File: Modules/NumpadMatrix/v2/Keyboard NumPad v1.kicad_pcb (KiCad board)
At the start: 2 copper layers, 80.2 x 123 mm, 57 parts, among them U2 ESP32-C3_SUPERMINI_SMD

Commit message: Update of Module V2  x_x
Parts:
- added ?: , , F.Cu at (45.9, 129.1)
- added ?: , , F.Cu at (84.0, 129.0)
- added ?: , , F.Cu at (64.9, 50.9)
- D26: moved to B.Cu
- moved D22 1.54 mm to (63.7, 138.9)
- turned S21 to 180 degrees
- turned S22 to 180 degrees
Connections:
- D27 pad 1: Linha 5 -> Linha 4
- S25 pad 1: Coluna 3 -> Coluna 4
- S26 pad 1: Coluna 3 -> Coluna 4
- S27 pad 1: Coluna 0 -> Coluna 4
- U2 pad 10: unconnected-(U2-GPIO10-Pad10) -> Coluna 4
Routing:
- net Coluna 4: track 0.00 -> 180.9 mm, vias 0 -> 4
- net Linha 4: track 162.0 -> 188.2 mm, vias 1 -> 2
- net Coluna 1: track 122.9 -> 137.5 mm, vias 2 -> 4
- net Linha 5: track 267.6 -> 257.9 mm
- net Net-(D21-A): track 3.95 -> 12.4 mm
- net Net-(D22-A): track 9.75 -> 17.5 mm
- net Coluna 0: track 133.9 -> 129.2 mm, vias 1 -> 2
- net Coluna 3: track 173.0 -> 176.2 mm
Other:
- board text added: "GND"

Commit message: fuck x_x
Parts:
- moved D5 3.25 mm to (42.6, 71.4), turned to 180 degrees
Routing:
- net Linha 0: track 23.3 -> 82.8 mm
- net Linha 5: track 257.9 -> 213.5 mm
- net Coluna 0: track 129.2 -> 155.6 mm, vias 2 -> 6
- net Coluna 1: track 137.5 -> 149.8 mm, vias 4 -> 5
- net Coluna 4: track 180.9 -> 169.6 mm, vias 4 -> 6
- net Coluna 3: track 176.2 -> 183.3 mm, vias 1 -> 2
- net Net-(D16-A): track 17.3 -> 24.2 mm, vias 1 -> 2
- net Net-(D5-A): track 14.7 -> 7.79 mm
- net Net-(D11-A): track 6.40 -> 13.0 mm, vias 0 -> 1
- net Net-(D4-A): track 6.20 -> 1.42 mm
- net Coluna 2: track 148.9 -> 144.3 mm
- net Net-(D25-A): track 0.00 -> 3.38 mm
- net Net-(D12-A): track 6.20 -> 3.42 mm
- net Net-(D1-A): track 6.56 -> 3.78 mm
- net Linha 4: track 188.2 -> 185.6 mm
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- removed copper zone on B.Cu, net (none)
- removed copper zone on F.Cu, net (none)

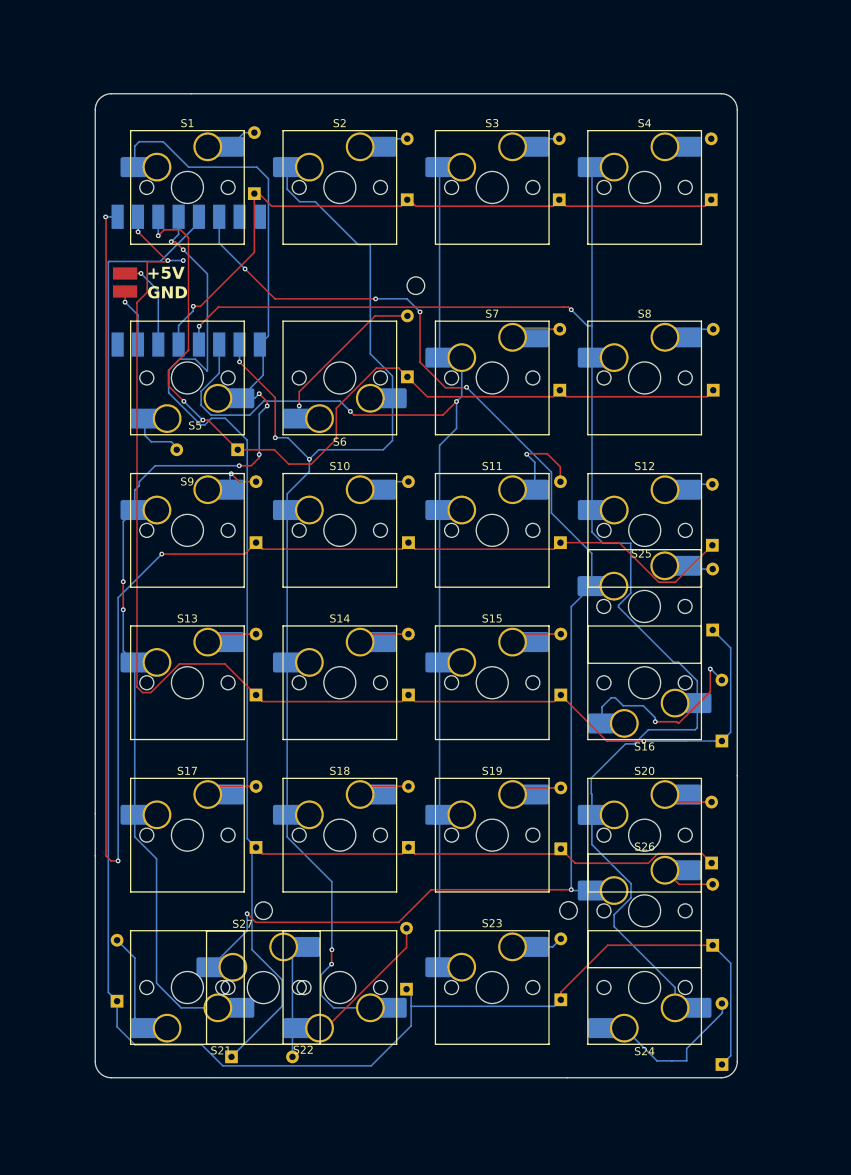
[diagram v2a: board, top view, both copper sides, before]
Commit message: Filled copper regions on the numpad module
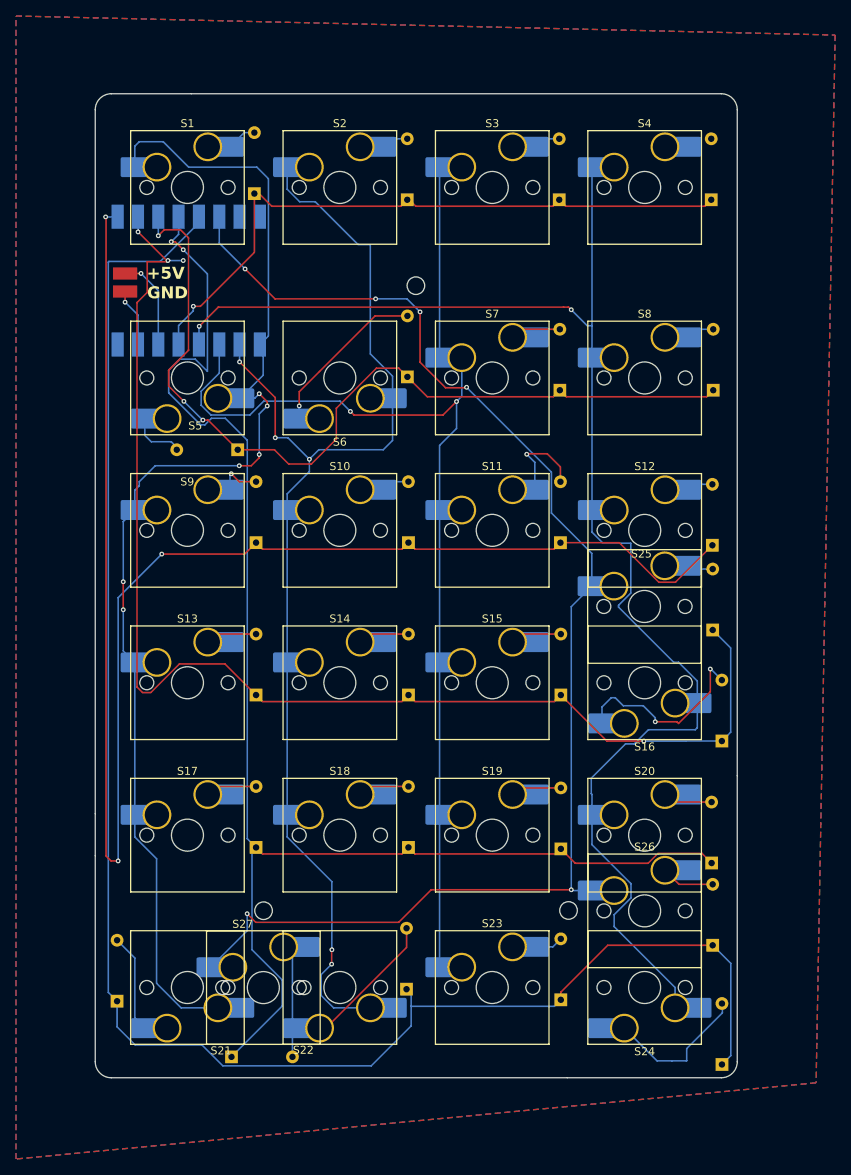
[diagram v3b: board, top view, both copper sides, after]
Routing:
- added copper zone on B.Cu, net (none)
- added copper zone on F.Cu, net (none)
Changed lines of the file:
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@@
 		(tags "Keyboard Keyswitch Switch Hotswap Socket Plated Relief Cutout Keycap 1.00u")
 		(property "Reference" "S12"
-			(at 0 -8 360)
+			(at 0 -8 0)
 			(layer "F.SilkS")
 			(effects
@@
 		)
 		(property "Value" "Keyswitch"
-			(at 0 8 360)
+			(at 0 8 0)
 			(layer "F.Fab")
 			(effects
@@
 		)
 		(property "Footprint" "ScottoKeebs_Hotswap:Hotswap_MX_Plated_1.00u"
-			(at 0 0 360)
+			(at 0 0 0)
 			(layer "F.Fab")
 			(hide yes)
@@
 		)
 		(property "Datasheet" ""
-			(at 0 0 360)
+			(at 0 0 0)
 			(layer "F.Fab")
 			(hide yes)
@@
 		)
 		(property "Description" "Push button switch, normally open, two pins, 45° tilted"
-			(at 0 0 360)
+			(at 0 0 0)
 			(layer "F.Fab")
 			(hide yes)
@@
 		)
 		(fp_text user "${REFERENCE}"
-			(at 0 0 360)
+			(at 0 0 0)
 			(layer "F.Fab")
 			(effects
@@
 		(tags "Diode DO-35_SOD27 series Axial Horizontal pin pitch 7.62mm  length 4mm diameter 2mm")
 		(property "Reference" "D5"
-			(at 3.81 -2 360)
+			(at 3.81 -2 0)
 			(layer "B.SilkS")
 			(effects
@@
 		)
 		(property "Value" "Diode"
-			(at 7 2.11 360)
+			(at 7 2.11 0)
 			(layer "B.Fab")
 			(hide yes)
@@
 		)
 		(fp_text user "K"
-			(at 0 1.85 360)
+			(at 0 1.85 0)
 			(layer "B.SilkS")
 			(effects
@@
 		)
 		(fp_text user "K"
-			(at 0 1.85 360)
+			(at 0 1.85 0)
 			(layer "B.Fab")
 			(effects
@@
 		)
 		(fp_text user "${REFERENCE}"
-			(at 4.11 0 360)
+			(at 4.11 0 0)
 			(layer "B.Fab")
 			(effects
@@
 		(net 43)
 	)
+	(zone
+		(net 0)
+		(net_name "")
+		(layers "F&B.Cu")
+		(hatch edge 0.5)
+		(connect_pads
+			(clearance 0.5)
+		)
+		(min_thickness 0.25)
+		(filled_areas_thickness no)
+		(fill yes
+			(thermal_gap 0.5)
+			(thermal_bridge_width 0.5)
+			(island_removal_mode 1)
+			(island_area_min 10)
+		)
+		(polygon
+			(pts
+				(xy 14.90375 17.21125) (xy 117.2975 19.5925) (xy 114.91625 150.56125) (xy 14.90375 160.08625)
+			)
+		)
+	)
 )

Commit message: fuck (again) x_x
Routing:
- net Coluna 1: track 149.8 -> 156.4 mm
- net Net-(D22-A): track 17.5 -> 22.7 mm, vias 0 -> 1
- net Net-(D13-A): track 6.45 -> 2.16 mm
- net Net-(D24-A): track 18.4 -> 22.7 mm
- net Coluna 0: track 155.6 -> 159.5 mm
- net Net-(D17-A): track 6.45 -> 10.1 mm
- net Coluna 3: track 183.3 -> 186.7 mm
- net Linha 4: track 185.6 -> 188.1 mm
- net Net-(D27-A): track 14.2 -> 15.8 mm
- net Net-(D19-A): track 6.38 -> 4.76 mm
- net Coluna 4: track 169.6 -> 171.1 mm
- net Net-(D20-A): track 6.22 -> 4.77 mm
- net Net-(D14-A): track 6.45 -> 5.09 mm
- net Net-(D15-A): track 6.45 -> 5.09 mm
- net Net-(D7-A): track 6.33 -> 4.97 mm
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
